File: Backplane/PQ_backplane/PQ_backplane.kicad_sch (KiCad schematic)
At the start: 12 parts, among them J1 M55-6002642R, J2 M55-6003242R, J3 M55-6002642R, J4 M55-6001242R, J5 USB4110-GF-A, U4 FUSB302BMPX

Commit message: Pushing changes to backplane
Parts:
- removed J2: M55-6003242R, inspireflyFootPrints:HARWIN_M55-6003242R, symbol inspireflySym:M55-6003242R
- added J2: FTSH-107-01-L-DV-K-A, inspireflyFootPrints:SAMTEC_FTSH-107-01-L-DV-K-A, symbol inspirefly:FTSH-107-01-L-DV-K-A
- added J6: M55-7104042R, inspireflyFootPrints:HARWIN_M55-7104042R, symbol inspirefly:M55-7104042R
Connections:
- net +3.3V: now also J3.B1, J3.B2, J3.B3, J2.03, J6.B17, J6.B18, J6.B19, J6.B20; no longer J3.A10, J3.A11, J3.A12, J3.A13
- net ANT_SPI2_MISO: now also J3.A2, J6.A11; no longer J3.B12
- net ANT_SPI2_MOSI: now also J3.A1, J6.A12; no longer J3.B13
- net ANT_SPI2_NSS: now also J3.A3, J6.A10; no longer J3.B11
- net ANT_SPI2_SCK: now also J3.A4, J6.A9; no longer J3.B10
- net BAT_HEAT_EN: now also J1.B8, J6.B10; no longer J1.B9
- net BURN_WIRE_EN: now also J3.A5, J6.A19; no longer J3.B9
- net CAN_H: now also J6.A16
- net CAN_L: now also J6.A14
- net DEBUG_LPUART_RX: now also J2.14, J6.B4
- net DEBUG_LPUART_TX: now also J2.13, J6.B3
- net EXTERNAL_VOLTAGE: now also J3.B10, J3.B11, J3.B12; no longer J3.A1, J3.A2, J3.A3, J3.A4
- net FOOTSWITCH: now also J6.B2
- net GND: now also J3.B4, J3.B5, J3.B6, J2.05, J2.07, J2.11, J6.A13, J6.A15, J6.A17, J6.A18, J6.B12, J6.B13, J6.B14, J6.B15, J6.B16, J6.SH1 (Shield), J6.SH2 (Shield), J6.SH3 (Shield), J6.SH4 (Shield); no longer J1.B11, J1.B12, J1.B13, J1.B6, J3.A5, J3.A6, J3.A7, J3.A8, J3.A9
- net I2C1_SCL: now also J3.A7, J6.A7; no longer J3.B7
- net I2C1_SDA: now also J3.A6, J6.A8; no longer J3.B8
- net I2C2_SCL: now also J1.B7, J3.A9, J6.A5; no longer J1.B8, J3.B5
- net I2C2_SDA: now also J1.B6, J3.A8, J6.A6; no longer J1.B7, J3.B6
- net I2C3_SCL: now also J3.A11, J6.A3; no longer J3.B3
- net I2C3_SDA: now also J3.A10, J6.A4; no longer J3.B4
- net I2C4_SCL: now also J3.A13, J6.A1; no longer J3.B1
- net I2C4_SDA: now also J3.A12, J6.A2; no longer J3.B2
- net JTCK/SWCLK: now also J2.06, J6.B8
- net JTDI: now also J2.10, J6.B6
- net JTMS/SWDIO: now also J2.04, J6.B9
- net NRST: now also J2.12, J6.B5
- net PAYLOAD_3.3V_EN: now also J1.B9, J6.B11; no longer J1.B10
- net SWO: now also J2.08, J6.B7
- net USBC_PD_INT_N: now also J6.A20
- new net BAT_VOLTAGE: J1.B10, J1.B11, J1.B12, J1.B13, J3.B7, J3.B8, J3.B9
- new net RFM_RESET: J3.B13, J6.B1
- no-connect marks 10 -> 13
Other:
- note added: "Debug for Flight Controller"
- moved on the sheet: J4

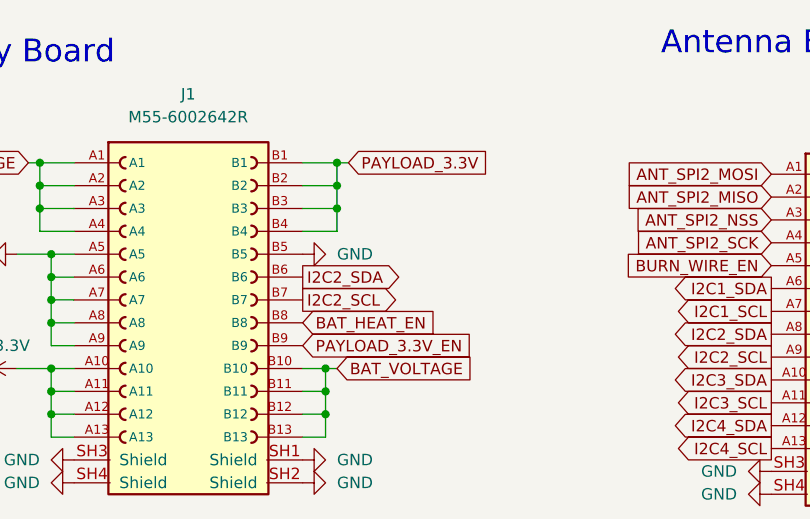
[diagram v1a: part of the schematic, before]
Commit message: Pushing Mainboard Split Up
Mainboard will be obsoleted soon

Battery Board and Flight Controller created

Battery Board - Good amount of routing done, additional area will be used for SuperCaps
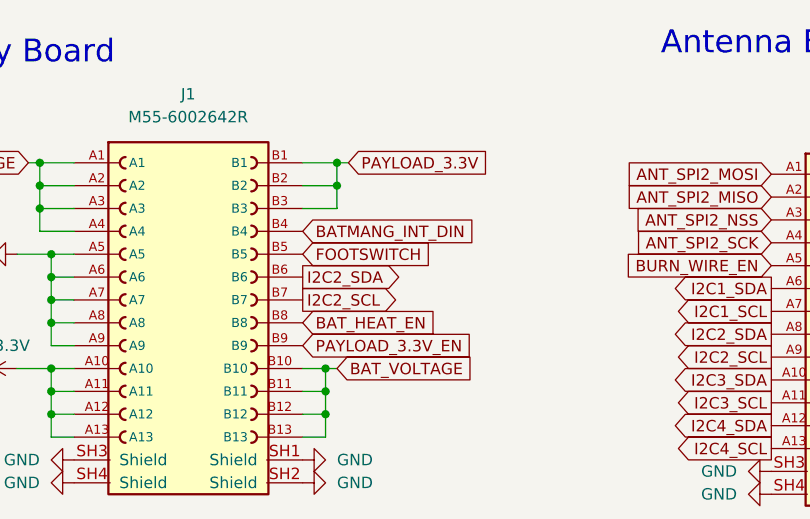
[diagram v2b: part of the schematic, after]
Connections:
- net FOOTSWITCH: now also J1.B5
- net GND: no longer J1.B5
- net PAYLOAD_3.3V: no longer J1.B4
- new net BATMANG_INT_DIN: J1.B4
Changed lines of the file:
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@@
 	)
 	(junction
-		(at 142.24 33.02)
-		(diameter 0)
-		(color 0 0 0 0)
-	)
-	(junction
 		(at 219.71 34.29)
 		(diameter 0)
@@
 	(wire
 		(pts
-			(xy 142.24 35.56) (xy 142.24 33.02)
-		)
-		(stroke
-			(width 0)
-			(type default)
-		)
-	)
-	(wire
-		(pts
 			(xy 54.61 114.3) (xy 54.61 116.84)
 		)
@@
 	(wire
 		(pts
-			(xy 138.43 35.56) (xy 142.24 35.56)
-		)
-		(stroke
-			(width 0)
-			(type default)
-		)
-	)
-	(wire
-		(pts
 			(xy 269.24 109.22) (xy 269.24 129.54)
 		)
@@
 		)
 	)
+	(global_label "BATMANG_INT_DIN"
+		(shape input)
+		(at 138.43 35.56 0)
+		(fields_autoplaced yes)
+		(effects
+			(font
+				(size 1.27 1.27)
+			)
+			(justify left)
+		)
+		(property "Intersheetrefs" "${INTERSHEET_REFS}"
+			(at 157.9253 35.56 0)
+			(effects
+				(font
+					(size 1.27 1.27)
+				)
+				(justify left)
+				(hide yes)
+			)
+		)
+	)
 	(global_label "I2C2_SDA"
 		(shape output)
@@
 		)
 	)
+	(global_label "FOOTSWITCH"
+		(shape input)
+		(at 138.43 38.1 0)
+		(fields_autoplaced yes)
+		(effects
+			(font
+				(size 1.27 1.27)
+			)
+			(justify left)
+		)
+		(property "Intersheetrefs" "${INTERSHEET_REFS}"
+			(at 152.9662 38.1 0)
+			(effects
+				(font
+					(size 1.27 1.27)
+				)
+				(justify left)
+				(hide yes)
+			)
+		)
+	)
 	(global_label "I2C2_SCL"
 		(shape output)
@@
 					(unit 1)
 				)
-			)
-		)
-	)
-	(symbol
-		(lib_id "power:GND")
-		(at 138.43 38.1 90)
-		(unit 1)
-		(exclude_from_sim no)
-		(in_bom yes)
-		(on_board yes)
-		(dnp no)
-		(fields_autoplaced yes)
-		(property "Reference" "#PWR021"
-			(at 144.78 38.1 0)
-			(effects
-				(font
-					(size 1.27 1.27)
-				)
-				(hide yes)
-			)
-		)
-		(property "Value" "GND"
-			(at 142.24 38.0999 90)
-			(effects
-				(font
-					(size 1.27 1.27)
-				)
-				(justify right)
-			)
-		)
-		(property "Footprint" ""
-			(at 138.43 38.1 0)
-			(effects
-				(font
-					(size 1.27 1.27)
-				)
-				(hide yes)
-			)
-		)
-		(property "Datasheet" ""
-			(at 138.43 38.1 0)
-			(effects
-				(font
-					(size 1.27 1.27)
-				)
-				(hide yes)
-			)
-		)
-		(property "Description" "Power symbol creates a global label with name \"GND\" , ground"
-			(at 138.43 38.1 0)
-			(effects
-				(font
-					(size 1.27 1.27)
-				)
-				(hide yes)
-			)
-		)
-		(pin "1"
-		)
-		(instances
-			(project "PQ_backplane"
-				(path "/e587a8f5-ffbc-4d9c-9649-3a36ea350c60"
-					(reference "#PWR021")
-					(unit 1)
-				)

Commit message: Flight Controller updates
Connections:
- net BATMANG_INT_DIN: now also J6.A18
- net BAT_VOLTAGE: no longer J1.B10
- net GND: no longer J6.A13, J6.A18
- new net ADC1_A1: J1.B10, J6.A13
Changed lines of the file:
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@@
 	)
 	(junction
-		(at 140.97 50.8)
-		(diameter 0)
-		(color 0 0 0 0)
-	)
-	(junction
 		(at 167.64 115.57)
 		(diameter 0)
@@
 	(wire
 		(pts
-			(xy 138.43 50.8) (xy 140.97 50.8)
-		)
-		(stroke
-			(width 0)
-			(type default)
-		)
-	)
-	(wire
-		(pts
 			(xy 91.44 88.9) (xy 142.24 88.9)
 		)
@@
 	(wire
 		(pts
-			(xy 140.97 53.34) (xy 140.97 50.8)
-		)
-		(stroke
-			(width 0)
-			(type default)
-		)
-	)
-	(wire
-		(pts
 			(xy 219.71 46.99) (xy 219.71 49.53)
 		)
@@
 	(wire
 		(pts
-			(xy 140.97 50.8) (xy 142.24 50.8)
+			(xy 140.97 53.34) (xy 142.24 53.34)
 		)
 		(stroke
@@
 	(global_label "BAT_VOLTAGE"
 		(shape input)
-		(at 142.24 50.8 0)
+		(at 142.24 53.34 0)
 		(fields_autoplaced yes)
 		(effects
@@
 		)
 		(property "Intersheetrefs" "${INTERSHEET_REFS}"
-			(at 157.4414 50.8 0)
+			(at 157.4414 53.34 0)
 			(effects
 				(font
@@
 		)
 	)
-	(global_label "BATMANG_INT_DIN"
-		(shape input)
-		(at 138.43 35.56 0)
-		(fields_autoplaced yes)
-		(effects
-			(font
-				(size 1.27 1.27)
-			)
-			(justify left)
-		)
-		(property "Intersheetrefs" "${INTERSHEET_REFS}"
-			(at 157.9253 35.56 0)
-			(effects
-				(font
-					(size 1.27 1.27)
-				)
-				(justify left)
-				(hide yes)
-			)
-		)
-	)
 	(global_label "I2C2_SDA"
 		(shape output)
@@
 		)
 	)
+	(global_label "BATMANG_INT_DIN"
+		(shape input)
+		(at 138.43 35.56 0)
+		(fields_autoplaced yes)
+		(effects
+			(font
+				(size 1.27 1.27)
+			)
+			(justify left)
+		)
+		(property "Intersheetrefs" "${INTERSHEET_REFS}"
+			(at 157.9253 35.56 0)
+			(effects
+				(font
+					(size 1.27 1.27)
+				)
+				(justify left)
+				(hide yes)
+			)
+		)
+	)
 	(global_label "USBC_PD_INT_N"
 		(shape output)
@@
 		)
 	)
+	(global_label "ADC1_A1"
+		(shape input)
+		(at 138.43 50.8 0)
+		(fields_autoplaced yes)
+		(effects
+			(font
+				(size 1.27 1.27)
+			)
+			(justify left)
+		)
+		(property "Intersheetrefs" "${INTERSHEET_REFS}"
+			(at 149.519 50.8 0)
+			(effects
+				(font
+					(size 1.27 1.27)
+				)
+				(justify left)
+				(hide yes)
+			)
+		)
+	)
 	(global_label "USBC_PD_INT_N"
 		(shape output)
@@
 		)
 	)
+	(global_label "ADC1_A1"
+		(shape input)
+		(at 60.96 57.15 0)
+		(fields_autoplaced yes)
+		(effects
+			(font
+				(size 1.27 1.27)
+			)
+			(justify left)
+		)
+		(property "Intersheetrefs" "${INTERSHEET_REFS}"
+			(at 72.049 57.15 0)
+			(effects
+				(font
+					(size 1.27 1.27)
+				)
+				(justify left)
+				(hide yes)
+			)
+		)
+	)
+	(global_label "BATMANG_INT_DIN"
+		(shape input)
+		(at 60.96 69.85 0)
+		(fields_autoplaced yes)
+		(effects
+			(font
+				(size 1.27 1.27)
+			)
+			(justify left)
+		)
+		(property "Intersheetrefs" "${INTERSHEET_REFS}"
+			(at 80.4553 69.85 0)
+			(effects
+				(font
+					(size 1.27 1.27)
+				)
+				(justify left)
+				(hide yes)
+			)
+		)
+	)
 	(global_label "ANT_SPI2_SCK"
 		(shape input)
@@
 	(symbol
 		(lib_id "power:GND")
-		(at 60.96 69.85 90)
-		(unit 1)
-		(exclude_from_sim no)
-		(in_bom yes)
-		(on_board yes)
-		(dnp no)
-		(fields_autoplaced yes)
-		(property "Reference" "#PWR09"
-			(at 67.31 69.85 0)
-			(effects
-				(font
-					(size 1.27 1.27)
-				)
-				(hide yes)
-			)
-		)
-		(property "Value" "GND"
-			(at 64.77 69.8499 90)
-			(effects
-				(font
-					(size 1.27 1.27)
-				)
-				(justify right)
-			)
-		)
-		(property "Footprint" ""
-			(at 60.96 69.85 0)
-			(effects
-				(font
-					(size 1.27 1.27)
-				)
-				(hide yes)
-			)
-		)
-		(property "Datasheet" ""
-			(at 60.96 69.85 0)
-			(effects
-				(font
-					(size 1.27 1.27)
-				)
-				(hide yes)
-			)
-		)
-		(property "Description" "Power symbol creates a global label with name \"GND\" , ground"
-			(at 60.96 69.85 0)
-			(effects
-				(font
-					(size 1.27 1.27)
-				)
-				(hide yes)
-			)
-		)
-		(pin "1"
-		)
-		(instances
-			(project "PQ_backplane"
-				(path "/e587a8f5-ffbc-4d9c-9649-3a36ea350c60"
-					(reference "#PWR09")
-					(unit 1)
-				)
-			)
-		)
-	)
-	(symbol
-		(lib_id "power:GND")
 		(at 52.07 120.65 90)
 		(unit 1)
@@
 					(unit 1)
 				)
-			)
-		)
-	)
-	(symbol
-		(lib_id "power:GND")
-		(at 60.96 57.15 90)
-		(unit 1)
-		(exclude_from_sim no)
-		(in_bom yes)
-		(on_board yes)
-		(dnp no)
-		(fields_autoplaced yes)
-		(property "Reference" "#PWR026"
-			(at 67.31 57.15 0)
-			(effects
-				(font
-					(size 1.27 1.27)
-				)
-				(hide yes)
-			)
-		)
-		(property "Value" "GND"
-			(at 64.77 57.1499 90)
-			(effects
-				(font
-					(size 1.27 1.27)
-				)
-				(justify right)
-			)
-		)
-		(property "Footprint" ""
-			(at 60.96 57.15 0)
-			(effects
-				(font
-					(size 1.27 1.27)
-				)
-				(hide yes)
-			)
-		)
-		(property "Datasheet" ""
-			(at 60.96 57.15 0)
-			(effects
-				(font
-					(size 1.27 1.27)
-				)
-				(hide yes)
-			)
-		)
-		(property "Description" "Power symbol creates a global label with name \"GND\" , ground"
-			(at 60.96 57.15 0)
-			(effects
-				(font
-					(size 1.27 1.27)
-				)
-				(hide yes)
-			)
-		)
-		(pin "1"
-		)
-		(instances
-			(project "PQ_backplane"
-				(path "/e587a8f5-ffbc-4d9c-9649-3a36ea350c60"
-					(reference "#PWR026")
-					(unit 1)
-				)

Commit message: Board sizes for FC and routing. slight Backplane changes
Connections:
- net GND: no longer J6.A17
- net PAYLOAD_3.3V: no longer J1.B3
- new net SUPER_CAP_CHARGE: J1.B3, J6.A17

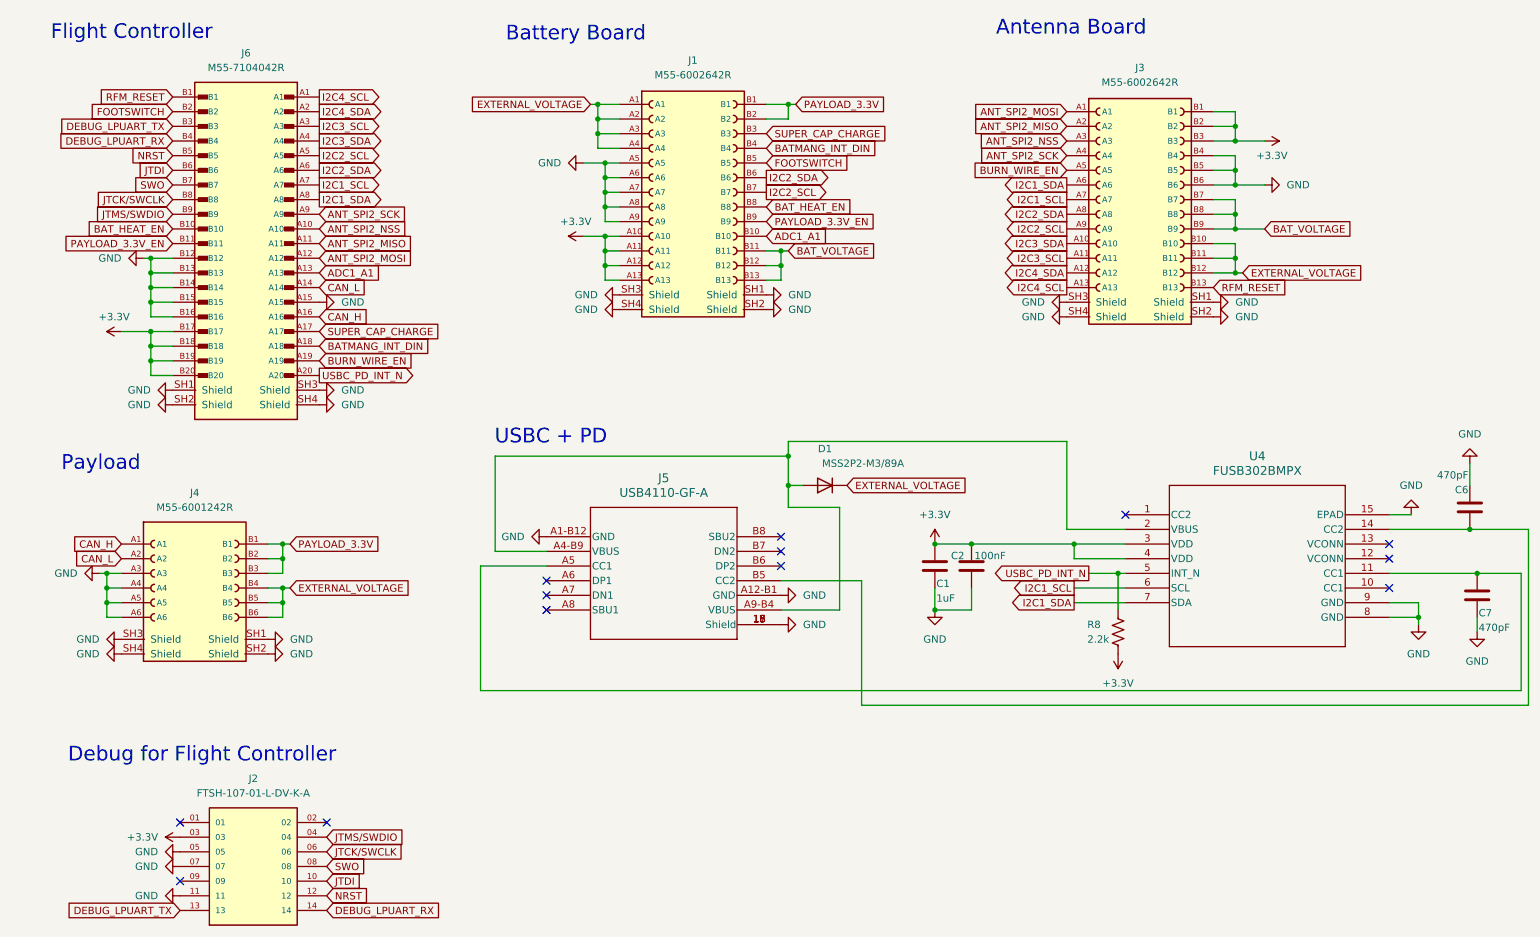
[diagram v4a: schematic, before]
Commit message: Routing and schematic work on most boards
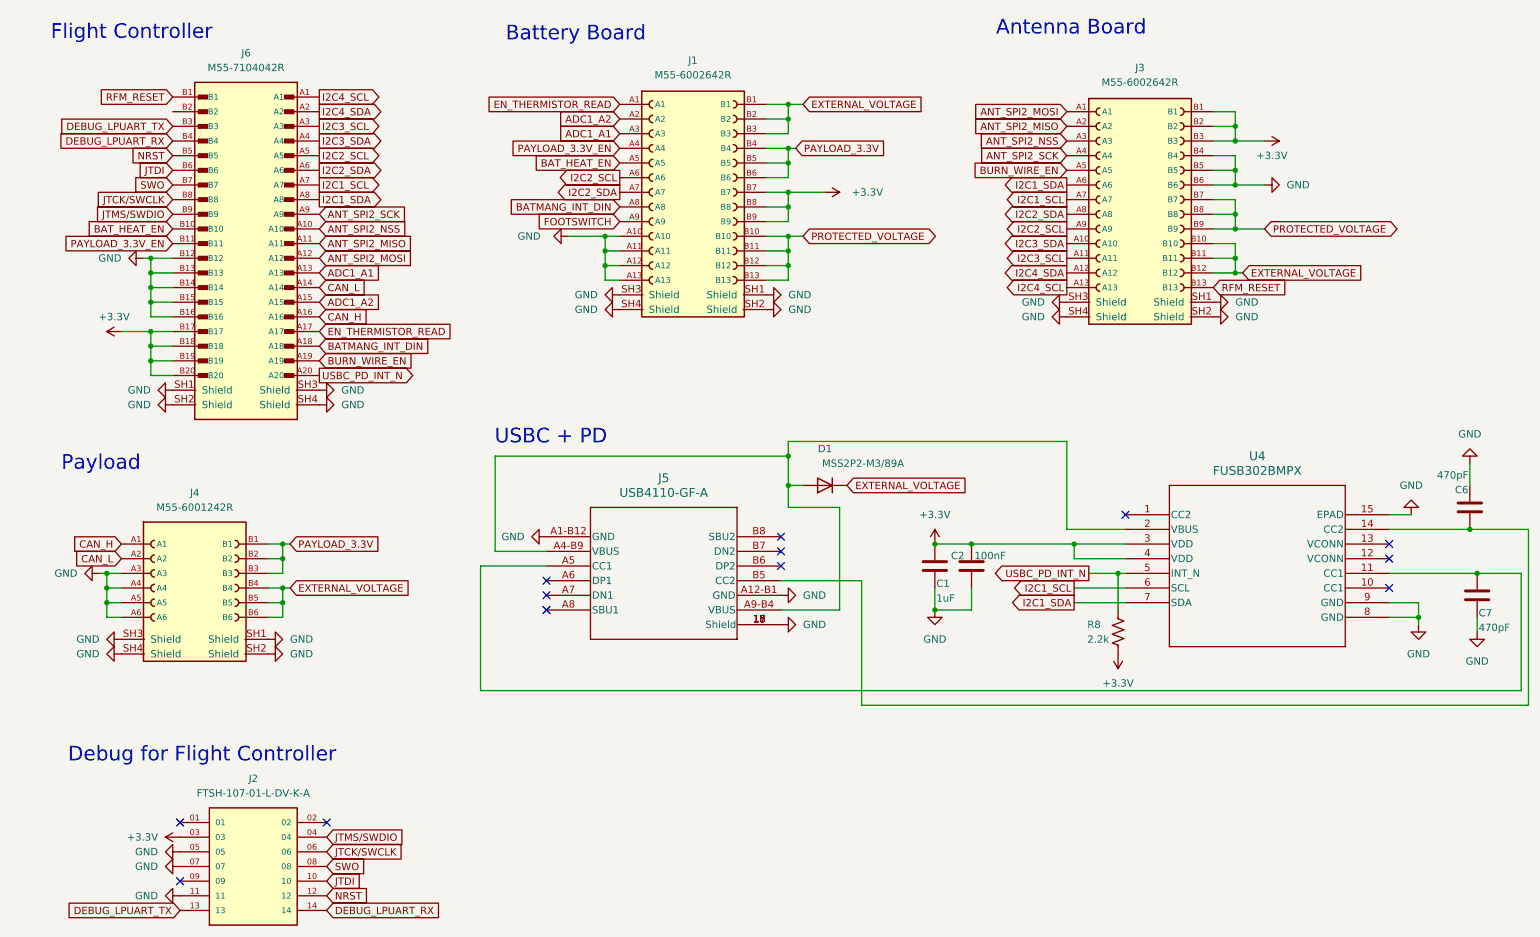
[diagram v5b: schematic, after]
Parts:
- J6: footprint inspireflyFootPrints:HARWIN_M55-7104042R -> inspireflyFootPrints:HARWIN_M55-6004042R
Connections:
- net +3.3V: now also J1.B7, J1.B8, J1.B9; no longer J1.A10, J1.A11, J1.A12, J1.A13
- net ADC1_A1: now also J1.A3; no longer J1.B10
- net BATMANG_INT_DIN: now also J1.A8; no longer J1.B4
- net BAT_HEAT_EN: now also J1.A5; no longer J1.B8
- net EXTERNAL_VOLTAGE: now also J1.B1, J1.B2, J1.B3; no longer J1.A1, J1.A2, J1.A3, J1.A4
- net FOOTSWITCH: now also J1.A9; no longer J1.B5, J6.B2
- net GND: now also J1.A10, J1.A11, J1.A12, J1.A13; no longer J1.A5, J1.A6, J1.A7, J1.A8, J1.A9, J6.A15
- net I2C2_SCL: now also J1.A6; no longer J1.B7
- net I2C2_SDA: now also J1.A7; no longer J1.B6
- net PAYLOAD_3.3V: now also J1.B4, J1.B5, J1.B6; no longer J1.B1, J1.B2
- net PAYLOAD_3.3V_EN: now also J1.A4; no longer J1.B9
- net BAT_VOLTAGE renamed PROTECTED_VOLTAGE
- net PROTECTED_VOLTAGE: now also J1.B10
- net SUPER_CAP_CHARGE renamed EN_THERMISTOR_READ
- net EN_THERMISTOR_READ: now also J1.A1; no longer J1.B3
- new net ADC1_A2: J1.A2, J6.A15
